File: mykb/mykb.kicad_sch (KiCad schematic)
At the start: 170 parts, among them J1 USB_C_Receptacle_USB2.0_16P, K0 Esc, K1 !,1, K10 ),0, K11 _,-, K12 +,=, K13 Backspace, K14 Home, K15 Tab, K16 Q, K17 W, K18 E, K19 R, K2 @,2, K20 T, K21 Y, K22 U, K23 I, K24 O, K25 P, K26 {,[, K27 },], K28 |,\, K29 PgUp, K3 #,3, K30 Caps Lock, K31 A, K32 S, K33 KeyD, K34 F, K35 G, K36 H, K37 J, K38 K, K39 L, K4 $,4, K40 :,;, K41 ",', K42 Enter, K43 PgDn, K44 Shift, K45 Z, K46 X, K47 KeyD, K48 V, K49 B, K5 %,5, K50 N, K51 M, K52 <,,, K53 >,., K54 ?,/, K55 Shift, K56 ↑, K57 End, K58 Ctrl, K59 Cmd, K6 ^,6, K60 Alt, K61 Blank, K62 Alt, K63 Ctrl, K64 ←, K65 ↓, K66 →, K7 &,7, K8 *,8, K9 (,9, SW1 SW_Push, SW2 SW_Push, SW3 RotaryEncoder_Switch_MP, SW4 RotaryEncoder_Switch_MP, U1 RP2040, U2 W25Q128JVS, U3 AMS1117-3.3, Y1 ABM8-272-T3

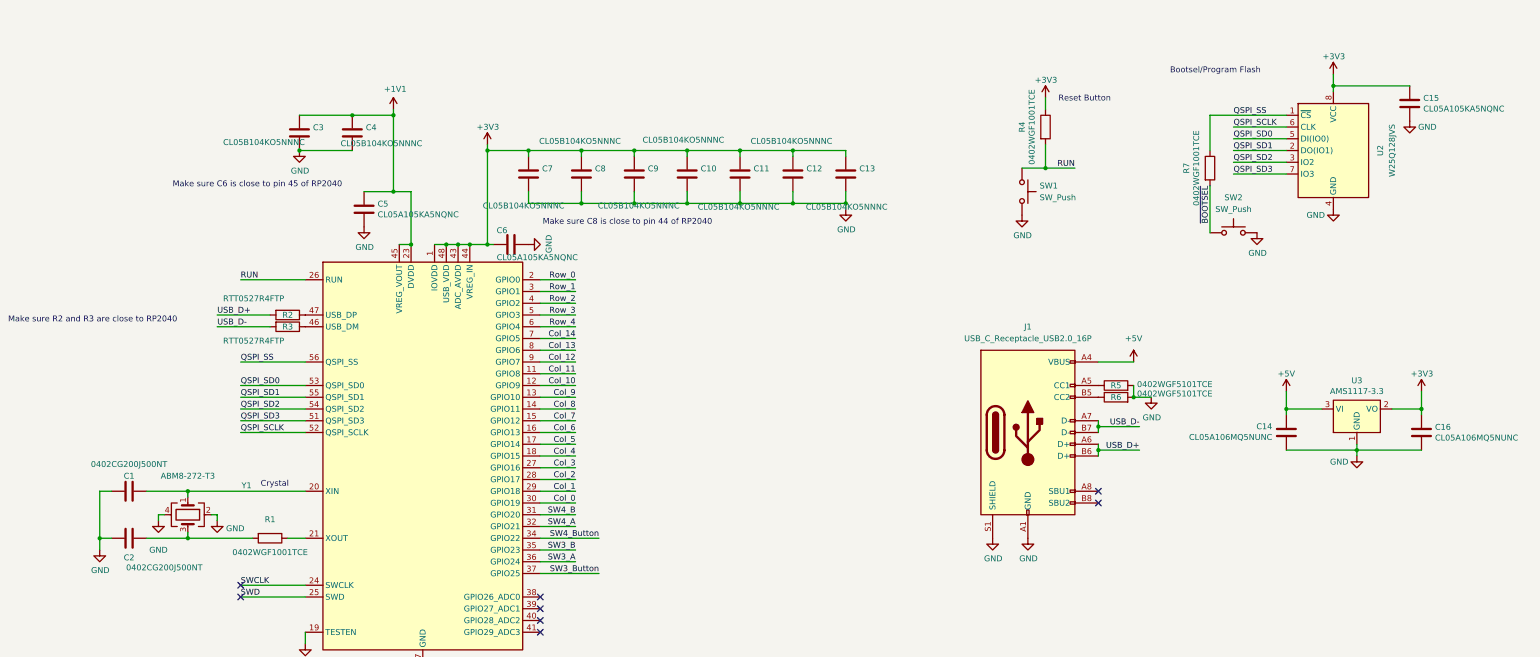
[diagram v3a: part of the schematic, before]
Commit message: move part nums to description
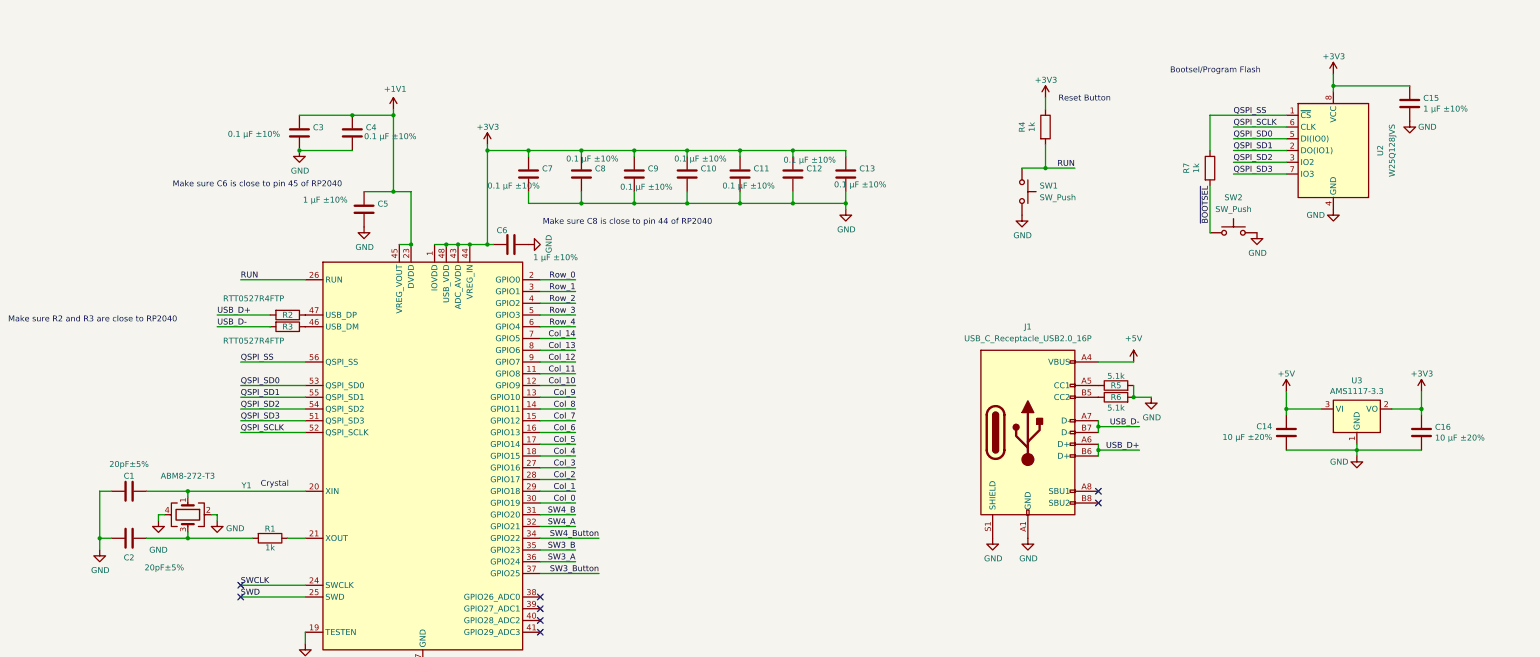
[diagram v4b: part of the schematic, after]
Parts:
- C1, C2: value 0402CG200J500NT -> 20pF±5%
- C10, C11, C12, C13, C3, C4, C7, C8, C9: value CL05B104KO5NNNC -> 0.1 µF ±10%
- C14, C16: value CL05A106MQ5NUNC -> 10 µF ±20%
- C15, C5, C6: value CL05A105KA5NQNC -> 1 µF ±10%
- R1, R4, R7: value 0402WGF1001TCE -> 1k
- R5, R6: value 0402WGF5101TCE -> 5.1k
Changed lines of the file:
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@@
 			)
 		)
-		(property "Value" "CL05B104KO5NNNC"
-			(at 215.138 123.444 0)
+		(property "Value" "0.1 µF ±10%"
+			(at 221.996 127.508 0)
 			(effects
 				(font
@@
 			)
 		)
-		(property "Datasheet" "~"
+		(property "Datasheet" "https://mm.digikey.com/Volume0/opasdata/d220001/medias/docus/609/CL05B104KO5NNNC.pdf"
 			(at 224.79 130.81 0)
 			(effects
@@
 			)
 		)
-		(property "Description" ""
+		(property "Description" "CL05B104KO5NNNC"
 			(at 224.79 130.81 0)
 			(effects
@@
 			)
 		)
-		(property "Value" "CL05A106MQ5NUNC"
+		(property "Value" "10 µF ±20%"
 			(at 386.461 187.833 0)
 			(effects
@@
 			)
 		)
-		(property "Datasheet" "~"
+		(property "Datasheet" "https://mm.digikey.com/Volume0/opasdata/d220001/medias/docus/41/CL05A106MQ5NUNC_Spec.pdf"
 			(at 383.54 186.69 0)
 			(effects
@@
 			)
 		)
-		(property "Description" ""
+		(property "Description" "CL05A106MQ5NUNC"
 			(at 383.54 186.69 0)
 			(effects
@@
 			)
 		)
-		(property "Value" "0402WGF5101TCE"
-			(at 330.2 178.308 90)
+		(property "Value" "5.1k"
+			(at 317.5 181.356 90)
 			(effects
 				(font
@@
 			)
 		)
-		(property "Datasheet" "~"
+		(property "Datasheet" "https://wmsc.lcsc.com/wmsc/upload/file/pdf/v2/lcsc/2206010045_UNI-ROYAL-Uniroyal-Elec-0402WGF5101TCE_C25905.pdf"
 			(at 317.5 179.07 0)
 			(effects
@@
 			)
 		)
-		(property "Description" "Resistor"
+		(property "Description" "0402WGF5101TCE"
 			(at 317.5 179.07 0)
 			(effects
@@
 			)
 		)
-		(property "Value" "0402WGF1001TCE"
+		(property "Value" "1k"
 			(at 299.3136 120.65 90)
 			(effects
@@
 			)
 		)
-		(property "Datasheet" "~"
+		(property "Datasheet" "https://www.mouser.com/datasheet/2/1365/1-3044649.pdf"
 			(at 302.26 120.65 0)
 			(effects
@@
 			)
 		)
-		(property "Description" ""
+		(property "Description" "0402WGF1001TCE"
 			(at 302.26 120.65 0)
 			(effects
@@
 			)
 		)
-		(property "Value" "CL05B104KO5NNNC"
-			(at 250.444 137.922 0)
+		(property "Value" "0.1 µF ±10%"
+			(at 256.54 133.096 0)
 			(effects
 				(font
@@
 			)
 		)
-		(property "Datasheet" "~"
+		(property "Datasheet" "https://mm.digikey.com/Volume0/opasdata/d220001/medias/docus/609/CL05B104KO5NNNC.pdf"
 			(at 259.08 130.81 0)
 			(effects
@@
 			)
 		)
-		(property "Description" ""
+		(property "Description" "CL05B104KO5NNNC"
 			(at 259.08 130.81 0)
 			(effects
@@
 			)
 		)
-		(property "Value" "CL05A105KA5NQNC"
+		(property "Value" "1 µF ±10%"
 			(at 201.168 148.844 90)
 			(effects
@@
 			)
 		)
-		(property "Datasheet" "~"
+		(property "Datasheet" "https://mm.digikey.com/Volume0/opasdata/d220001/medias/docus/41/CL05A105KA5NQNC.pdf"
 			(at 186.69 146.05 0)
 			(effects
@@
 			)
 		)
-		(property "Description" ""
+		(property "Description" "CL05A105KA5NQNC"
 			(at 186.69 146.05 0)
 			(effects
@@
 			)
 		)
-		(property "Value" "CL05B104KO5NNNC"
-			(at 238.506 123.698 0)
+		(property "Value" "0.1 µF ±10%"
+			(at 245.618 127.762 0)
 			(effects
 				(font
@@
 			)
 		)
-		(property "Datasheet" "~"
+		(property "Datasheet" "https://mm.digikey.com/Volume0/opasdata/d220001/medias/docus/609/CL05B104KO5NNNC.pdf"
 			(at 247.65 130.81 0)
 			(effects
@@
 			)
 		)
-		(property "Description" ""
+		(property "Description" "CL05B104KO5NNNC"
 			(at 247.65 130.81 0)
 			(effects
@@
 			)
 		)
-		(property "Value" "0402CG200J500NT"
+		(property "Value" "20pF±5%"
 			(at 104.14 193.5511 90)
 			(effects
@@
 			)
 		)
-		(property "Datasheet" "~"
+		(property "Datasheet" "https://www.lcsc.com/datasheet/lcsc_datasheet_2304140030_FH--Guangdong-Fenghua-Advanced-Tech-0402CG200J500NT_C1554.pdf"
 			(at 104.14 199.39 0)
 			(effects
@@
 			)
 		)
-		(property "Description" ""
+		(property "Description" "0402CG200J500NT"
 			(at 104.14 199.39 0)
 			(effects
@@
 			)
 		)
-		(property "Value" "0402CG200J500NT"
+		(property "Value" "20pF±5%"
 			(at 111.76 215.9 90)
 			(effects
@@
 			)
 		)
-		(property "Datasheet" "~"
+		(property "Datasheet" "https://www.lcsc.com/datasheet/lcsc_datasheet_2304140030_FH--Guangdong-Fenghua-Advanced-Tech-0402CG200J500NT_C1554.pdf"
 			(at 104.14 209.55 0)
 			(effects
@@
 			)
 		)
-		(property "Description" ""
+		(property "Description" "0402CG200J500NT"
 			(at 104.14 209.55 0)
 			(effects
@@
 			)
 		)
-		(property "Value" "CL05A105KA5NQNC"
-			(at 157.861 139.573 0)
+		(property "Value" "1 µF ±10%"
+			(at 141.732 136.398 0)
 			(effects
 				(font
@@
 			)
 		)
-		(property "Datasheet" "~"
+		(property "Datasheet" "https://mm.digikey.com/Volume0/opasdata/d220001/medias/docus/41/CL05A105KA5NQNC.pdf"
 			(at 154.94 138.43 0)
 			(effects
@@
 			)
 		)
-		(property "Description" ""
+		(property "Description" "CL05A105KA5NQNC"
 			(at 154.94 138.43 0)
 			(effects
@@
 			)
 		)
-		(property "Value" "CL05A105KA5NQNC"
+		(property "Value" "1 µF ±10%"
 			(at 383.921 116.713 0)
 			(effects
@@
 			)
 		)
-		(property "Datasheet" "~"
+		(property "Datasheet" "https://mm.digikey.com/Volume0/opasdata/d220001/medias/docus/41/CL05A105KA5NQNC.pdf"
 			(at 381 115.57 0)
 			(effects
@@
 			)
 		)
-		(property "Description" ""
+		(property "Description" "CL05A105KA5NQNC"
 			(at 381 115.57 0)
 			(effects
@@
 			)
 		)
-		(property "Value" "CL05B104KO5NNNC"
-			(at 124.46 123.952 0)
+		(property "Value" "0.1 µF ±10%"
+			(at 125.476 122.174 0)
 			(effects
 				(font
@@
 			)
 		)
-		(property "Datasheet" "~"
+		(property "Datasheet" "https://mm.digikey.com/Volume0/opasdata/d220001/medias/docus/609/CL05B104KO5NNNC.pdf"
 			(at 140.97 121.92 0)
 			(effects
@@
 			)
 		)
-		(property "Description" ""
+		(property "Description" "CL05B104KO5NNNC"
 			(at 140.97 121.92 0)
 			(effects
@@
 		(dnp no)
 		(property "Reference" "R1"
-			(at 134.62 205.486 90)
+			(at 134.62 207.518 90)
 			(effects
 				(font
@@
 			)
 		)
-		(property "Value" "0402WGF1001TCE"
-			(at 134.62 212.598 90)
+		(property "Value" "1k"
+			(at 134.62 211.582 90)
 			(effects
 				(font
@@
 			)
 		)
-		(property "Datasheet" "~"
+		(property "Datasheet" "https://www.mouser.com/datasheet/2/1365/1-3044649.pdf"
 			(at 134.62 209.55 0)
 			(effects
@@
 			)
 		)
-		(property "Description" ""
+		(property "Description" "0402WGF1001TCE"
 			(at 134.62 209.55 0)
 			(effects
@@
 			)
 		)
-		(property "Value" "CL05A106MQ5NUNC"
+		(property "Value" "10 µF ±20%"
 			(at 351.282 187.706 0)
 			(effects
@@
 			)
 		)
-		(property "Datasheet" "~"
+		(property "Datasheet" "https://mm.digikey.com/Volume0/opasdata/d220001/medias/docus/41/CL05A106MQ5NUNC_Spec.pdf"
 			(at 354.33 186.69 0)
 			(effects
@@
 			)
 		)
-		(property "Description" ""
+		(property "Description" "CL05A106MQ5NUNC"
 			(at 354.33 186.69 0)
 			(effects
@@
 			)
 		)
-		(property "Value" "0402WGF1001TCE"
+		(property "Value" "1k"
 			(at 334.8736 129.54 90)
 			(effects
@@
 			)
 		)
-		(property "Datasheet" "~"
+		(property "Datasheet" "https://www.mouser.com/datasheet/2/1365/1-3044649.pdf"
 			(at 337.82 129.54 0)
 			(effects
@@
 			)
 		)
-		(property "Description" ""
+		(property "Description" "0402WGF1001TCE"
 			(at 337.82 129.54 0)
 			(effects
@@
 			)
 		)
-		(property "Value" "CL05B104KO5NNNC"
-			(at 227.076 137.922 0)
+		(property "Value" "0.1 µF ±10%"
+			(at 232.41 133.35 0)
 			(effects
 				(font
@@
 			)
 		)
-		(property "Datasheet" "~"
+		(property "Datasheet" "https://mm.digikey.com/Volume0/opasdata/d220001/medias/docus/609/CL05B104KO5NNNC.pdf"
 			(at 236.22 130.81 0)
 			(effects
@@
 			)
 		)
-		(property "Description" ""
+		(property "Description" "CL05B104KO5NNNC"
 			(at 236.22 130.81 0)
 			(effects
@@
 			)
 		)
-		(property "Value" "CL05B104KO5NNNC"
-			(at 180.594 137.668 0)
+		(property "Value" "0.1 µF ±10%"
+			(at 181.61 133.35 0)
 			(effects
 				(font
@@
 			)
 		)
-		(property "Datasheet" "~"
+		(property "Datasheet" "https://mm.digikey.com/Volume0/opasdata/d220001/medias/docus/609/CL05B104KO5NNNC.pdf"
 			(at 190.5 130.81 0)
 			(effects
@@
 			)
 		)
-		(property "Description" ""
+		(property "Description" "CL05B104KO5NNNC"
 			(at 190.5 130.81 0)
 			(effects
@@
 			)
 		)
-		(property "Value" "CL05B104KO5NNNC"
-			(at 205.486 137.668 0)
+		(property "Value" "0.1 µF ±10%"
+			(at 210.312 133.604 0)
 			(effects
 				(font
@@
 			)
 		)
-		(property "Datasheet" "~"
+		(property "Datasheet" "https://mm.digikey.com/Volume0/opasdata/d220001/medias/docus/609/CL05B104KO5NNNC.pdf"
 			(at 213.36 130.81 0)
 			(effects
@@
 			)
 		)
-		(property "Description" ""
+		(property "Description" "CL05B104KO5NNNC"
 			(at 213.36 130.81 0)
 			(effects
@@
 			)
 		)
-		(property "Value" "CL05B104KO5NNNC"
-			(at 149.86 124.206 0)
+		(property "Value" "0.1 µF ±10%"
+			(at 154.94 122.682 0)
 			(effects
 				(font
@@
 			)
 		)
-		(property "Datasheet" "~"
+		(property "Datasheet" "https://mm.digikey.com/Volume0/opasdata/d220001/medias/docus/609/CL05B104KO5NNNC.pdf"
 			(at 152.4 121.92 0)
 			(effects
@@
 			)
 		)
-		(property "Description" ""
+		(property "Description" "CL05B104KO5NNNC"
 			(at 152.4 121.92 0)
 			(effects
@@
 			)
 		)
-		(property "Value" "CL05B104KO5NNNC"
-			(at 192.786 123.698 0)
+		(property "Value" "0.1 µF ±10%"
+			(at 198.628 127.508 0)
 			(effects
 				(font
@@
 			)
 		)
-		(property "Datasheet" "~"
+		(property "Datasheet" "https://mm.digikey.com/Volume0/opasdata/d220001/medias/docus/609/CL05B104KO5NNNC.pdf"
 			(at 201.93 130.81 0)
 			(effects
@@
 			)
 		)
-		(property "Description" ""
+		(property "Description" "CL05B104KO5NNNC"
 			(at 201.93 130.81 0)
 			(effects
@@
 			)
 		)
-		(property "Value" "0402WGF5101TCE"
-			(at 330.2 176.276 90)
+		(property "Value" "5.1k"
+			(at 317.5 174.498 90)
 			(effects
 				(font
@@
 			)
 		)
-		(property "Datasheet" "~"
+		(property "Datasheet" "https://wmsc.lcsc.com/wmsc/upload/file/pdf/v2/lcsc/2206010045_UNI-ROYAL-Uniroyal-Elec-0402WGF5101TCE_C25905.pdf"
 			(at 317.5 176.53 0)
 			(effects
@@
 			)
 		)
-		(property "Description" "Resistor"
+		(property "Description" "0402WGF5101TCE"
 			(at 317.5 176.53 0)
 			(effects
